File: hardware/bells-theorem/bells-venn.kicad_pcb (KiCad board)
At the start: 2 copper layers, 257.4 x 128.5 mm, 312 parts, among them J1 Conn_02x05_Odd_Even, J10 D, J11 C, J12 DA, J13 CD, J14 DAB, J15 CDA, J16 A, J17 B, J18 AB, J19 BC, J2 left, J20 ABC, J21 BCD, J22 left, J23 right, J3 right, J4 IN, J5 CVA, J6 CVB, J7 CVC, J8 CVD, J9 ABCD, Q1 Q_NPN_BCE, Q10 Q_NPN_BCE, Q12 Q_NPN_BCE, Q13 Q_NPN_BCE, Q3 Q_NPN_BCE, Q4 Q_NPN_BCE, Q6 Q_NPN_BCE, Q7 Q_NPN_BCE, Q9 Q_NPN_BCE, SW1 A, SW2 D, SW3 B, SW4 C, U1 Teensy4.1, U10 MCP47CVB12, U11 MCP47CVB12, U12 TL074, U13 TL074, U14 TL074, U15 TL072, U16 TL074, U17 TL074, U18 TL074, U19 TL074, U2 L7805, U20 TL074, U21 TL072, U3 L78L33_TO92, U4 PI4MSD5V9540B, U5 MCP47CVB11, U6 MCP47CVB12, U7 MCP47CVB12, U8 MCP47CVB12, U9 MCP47CVB12

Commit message: take gerbers out of the repo, push latest updates
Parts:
- removed the G*** at (60.7, 82.0)
- removed the G*** at (150.7, 81.9)
- removed the G*** at (60.7, 81.9)
- removed the REF** at (37.8, 36.1)
- removed the REF** at (83.3, 36.1)
- removed the REF** at (83.3, 80.7)
- removed the REF** at (258.1, 106.8)
- removed the REF** at (266.1, 102.0)
- removed the REF** at (216.3, 109.6)
- removed the REF** at (216.9, 101.7)
- removed the REF** at (37.8, 80.7)
- removed the REF** at (202.1, 109.0)
- removed the REF** at (203.8, 49.7)
- removed the REF** at (216.2, 43.4)
- removed the REF** at (204.5, 62.2)
- removed the REF** at (206.1, 75.8)
- removed the REF** at (217.4, 80.8)
- removed the REF** at (214.1, 84.6)
- removed the REF** at (214.2, 67.2)
- removed the REF** at (217.3, 56.4)
- removed the REF** at (214.1, 48.8)
- removed the REF** at (60.5, 80.8)
- removed the REF** at (219.5, 38.0)
- removed the REF** at (213.2, 31.1)
- removed the REF** at (218.4, 31.1)
- removed the REF** at (223.6, 31.1)
- removed the REF** at (265.7, 32.3)
- removed the REF** at (238.8, 38.2)
- removed the REF** at (244.9, 31.1)
- removed the REF** at (258.8, 31.2)
- removed the REF** at (254.3, 31.1)
- removed the REF** at (249.7, 31.2)
- removed the REF** at (250.7, 38.1)
- removed the REF** at (255.3, 38.2)
- removed the REF** at (274.4, 52.8)
- removed the REF** at (257.3, 42.0)
- removed the REF** at (257.4, 69.6)
- removed the REF** at (258.1, 85.2)
- removed the REF** at (257.3, 53.8)
- removed the REF** at (273.1, 60.1)
- removed the REF** at (273.1, 57.7)
- removed the REF** at (257.4, 58.8)
- removed the REF** at (262.1, 46.0)
- removed the REF** at (260.5, 49.7)
- removed the REF** at (262.4, 73.2)
- removed the REF** at (260.5, 77.0)
- removed the REF** at (262.9, 88.8)
- removed the REF** at (261.2, 92.7)
- removed SW1: A, Rotary_Encoder:RotaryEncoder_Alps_EC12E-Switch_Vertical_H20mm_CircularMountingHoles
- removed SW2: D, Rotary_Encoder:RotaryEncoder_Alps_EC12E-Switch_Vertical_H20mm_CircularMountingHoles
- removed SW3: B, Rotary_Encoder:RotaryEncoder_Alps_EC12E-Switch_Vertical_H20mm_CircularMountingHoles
- removed SW4: C, Rotary_Encoder:RotaryEncoder_Alps_EC12E-Switch_Vertical_H20mm_CircularMountingHoles
- removed U11: MCP47CVB12, Package_SO:MSOP-10_3x3mm_P0.5mm
- removed U12, U13, U14, U16, U17, U18: TL074, Package_SO:SOIC-14_3.9x8.7mm_P1.27mm
- removed U15: TL072, Package_SO:SOIC-8_3.9x4.9mm_P1.27mm
- added C10: 15nF, Capacitor_SMD:C_0805_2012Metric_Pad1.15x1.40mm_HandSolder, B.Cu at (253.5, 61.2)
- added C11: 15nF, Capacitor_SMD:C_0805_2012Metric_Pad1.15x1.40mm_HandSolder, B.Cu at (253.5, 79.0)
- added C12: 15nF, Capacitor_SMD:C_0805_2012Metric_Pad1.15x1.40mm_HandSolder, B.Cu at (253.5, 89.2)
- added C13: 15nF, Capacitor_SMD:C_0805_2012Metric_Pad1.15x1.40mm_HandSolder, B.Cu at (253.5, 66.0)
- added C14: 100nF, Capacitor_SMD:C_0805_2012Metric_Pad1.15x1.40mm_HandSolder, B.Cu at (261.9, 34.5)
- added C35: 100nF, Capacitor_SMD:C_0805_2012Metric_Pad1.15x1.40mm_HandSolder, B.Cu at (217.9, 47.2)
- added C36: 100nF, Capacitor_SMD:C_0805_2012Metric_Pad1.15x1.40mm_HandSolder, B.Cu at (217.9, 35.6)
- added C37: 100nF, Capacitor_SMD:C_0805_2012Metric_Pad1.15x1.40mm_HandSolder, B.Cu at (217.9, 65.3)
- added C38: 100nF, Capacitor_SMD:C_0805_2012Metric_Pad1.15x1.40mm_HandSolder, B.Cu at (217.9, 53.6)
- added C39: 100nF, Capacitor_SMD:C_0805_2012Metric_Pad1.15x1.40mm_HandSolder, B.Cu at (217.9, 81.5)
- added C7: 15nF, Capacitor_SMD:C_0805_2012Metric_Pad1.15x1.40mm_HandSolder, B.Cu at (253.3, 35.1)
- added C8: 15nF, Capacitor_SMD:C_0805_2012Metric_Pad1.15x1.40mm_HandSolder, B.Cu at (253.5, 51.1)
- added C9: 15nF, Capacitor_SMD:C_0805_2012Metric_Pad1.15x1.40mm_HandSolder, B.Cu at (253.4, 45.5)
- added G***: LOGO, My Library:bells-theorem-trefoil, F.Cu at (60.8, 58.3)
- added G***: LOGO, My Library:bells-theorem-just-inside-bmask, F.Cu at (60.8, 58.3)
- added G***: LOGO, My Library:bells-theorem-just-inside-fmask, F.Cu at (60.8, 58.3)
- added Q11: 2N3904, Package_TO_SOT_SMD:SOT-23_Handsoldering, F.Cu at (166.0, 91.2)
- added Q2: 2N3904, Package_TO_SOT_SMD:SOT-23_Handsoldering, F.Cu at (118.4, 48.7)
- added Q5: 2N3904, Package_TO_SOT_SMD:SOT-23_Handsoldering, F.Cu at (122.2, 91.2)
- added Q8: 2N3904, Package_TO_SOT_SMD:SOT-23_Handsoldering, F.Cu at (176.5, 47.4)
- added R11: 10K, Resistor_SMD:R_0805_2012Metric_Pad1.15x1.40mm_HandSolder, B.Cu at (253.4, 39.1)
- added R131: 390R, Resistor_SMD:R_0805_2012Metric_Pad1.15x1.40mm_HandSolder, F.Cu at (119.2, 43.8)
- added R14: 10K, Resistor_SMD:R_0805_2012Metric_Pad1.15x1.40mm_HandSolder, B.Cu at (253.4, 41.4)
- added R17: 10K, Resistor_SMD:R_0805_2012Metric_Pad1.15x1.40mm_HandSolder, B.Cu at (253.5, 55.1)
- added R20: 10K, Resistor_SMD:R_0805_2012Metric_Pad1.15x1.40mm_HandSolder, B.Cu at (253.5, 57.1)
- added R23: 10K, Resistor_SMD:R_0805_2012Metric_Pad1.15x1.40mm_HandSolder, B.Cu at (253.5, 83.1)
- added R26: 10K, Resistor_SMD:R_0805_2012Metric_Pad1.15x1.40mm_HandSolder, B.Cu at (253.5, 85.1)
- added R29: 10K, Resistor_SMD:R_0805_2012Metric_Pad1.15x1.40mm_HandSolder, B.Cu at (253.5, 70.6)
- added R32: 30K, Resistor_SMD:R_0805_2012Metric_Pad1.15x1.40mm_HandSolder, B.Cu at (253.4, 37.1)
- added REF**: stitch-via-0.6mm, My Library:stitch-via-0.6mm, F.Cu at (169.1, 90.2)
- added REF**: MountingHole_9mm_dia, My Library:MountingHole_9mm_dia, F.Cu at (38.3, 80.7)
- added REF**: MountingHole_9mm_dia, My Library:MountingHole_9mm_dia, F.Cu at (38.3, 35.8)
- added REF**: stitch-via-0.6mm, My Library:stitch-via-0.6mm, F.Cu at (260.9, 122.0)
- added REF**: stitch-via-0.6mm, My Library:stitch-via-0.6mm, F.Cu at (213.4, 113.4)
- added REF**: stitch-via-0.6mm, My Library:stitch-via-0.6mm, F.Cu at (246.9, 32.5)
- added REF**: stitch-via-0.6mm, My Library:stitch-via-0.6mm, F.Cu at (225.4, 87.8)
- added REF**: stitch-via-0.6mm, My Library:stitch-via-0.6mm, F.Cu at (263.9, 100.8)
- added REF**: stitch-via-0.6mm, My Library:stitch-via-0.6mm, F.Cu at (264.7, 95.8)
- added REF**: stitch-via-0.6mm, My Library:stitch-via-0.6mm, F.Cu at (205.5, 74.4)
- added REF**: stitch-via-0.6mm, My Library:stitch-via-0.6mm, F.Cu at (214.1, 66.5)
- added REF**: stitch-via-0.6mm, My Library:stitch-via-0.6mm, F.Cu at (206.2, 64.3)
- added REF**: stitch-via-0.6mm, My Library:stitch-via-0.6mm, F.Cu at (206.0, 55.1)
- added REF**: stitch-via-0.6mm, My Library:stitch-via-0.6mm, F.Cu at (212.1, 58.7)
- added REF**: stitch-via-0.6mm, My Library:stitch-via-0.6mm, F.Cu at (234.2, 89.7)
- added REF**: stitch-via-0.6mm, My Library:stitch-via-0.6mm, F.Cu at (218.7, 98.3)
- added REF**: stitch-via-0.6mm, My Library:stitch-via-0.6mm, F.Cu at (219.2, 52.3)
- added REF**: stitch-via-0.6mm, My Library:stitch-via-0.6mm, F.Cu at (213.1, 91.2)
- added REF**: stitch-via-0.6mm, My Library:stitch-via-0.6mm, F.Cu at (217.4, 85.1)
- added REF**: stitch-via-0.6mm, My Library:stitch-via-0.6mm, F.Cu at (214.6, 74.4)
- added REF**: MountingHole_9mm_dia, My Library:MountingHole_9mm_dia, F.Cu at (83.2, 80.7)
- added REF**: stitch-via-0.6mm, My Library:stitch-via-0.6mm, F.Cu at (220.2, 66.0)
- added REF**: stitch-via-0.6mm, My Library:stitch-via-0.6mm, F.Cu at (219.7, 60.5)
- added REF**: stitch-via-0.6mm, My Library:stitch-via-0.6mm, F.Cu at (218.9, 48.8)
- added REF**: stitch-via-0.6mm, My Library:stitch-via-0.6mm, F.Cu at (214.6, 40.1)
- added REF**: stitch-via-0.6mm, My Library:stitch-via-0.6mm, F.Cu at (258.8, 100.3)
- added REF**: stitch-via-0.6mm, My Library:stitch-via-0.6mm, F.Cu at (258.6, 82.8)
- added REF**: stitch-via-0.6mm, My Library:stitch-via-0.6mm, F.Cu at (258.6, 73.9)
- added REF**: stitch-via-0.6mm, My Library:stitch-via-0.6mm, F.Cu at (262.9, 32.8)
- added REF**: stitch-via-0.6mm, My Library:stitch-via-0.6mm, F.Cu at (262.9, 64.0)
- added REF**: stitch-via-0.6mm, My Library:stitch-via-0.6mm, F.Cu at (262.9, 48.3)
- added REF**: stitch-via-0.6mm, My Library:stitch-via-0.6mm, B.Cu at (258.6, 54.9)
- added REF**: stitch-via-0.6mm, My Library:stitch-via-0.6mm, F.Cu at (259.0, 39.1)
- added REF**: stitch-via-0.6mm, My Library:stitch-via-0.6mm, F.Cu at (161.6, 86.4)
- added REF**: stitch-via-0.6mm, My Library:stitch-via-0.6mm, F.Cu at (113.6, 37.7)
- added REF**: stitch-via-0.6mm, My Library:stitch-via-0.6mm, F.Cu at (144.4, 78.7)
- added REF**: stitch-via-0.6mm, My Library:stitch-via-0.6mm, F.Cu at (137.6, 67.7)
- added REF**: stitch-via-0.6mm, My Library:stitch-via-0.6mm, F.Cu at (178.6, 84.8)
- added REF**: stitch-via-0.6mm, My Library:stitch-via-0.6mm, F.Cu at (173.2, 90.8)
- added REF**: MountingHole_9mm_dia, My Library:MountingHole_9mm_dia, F.Cu at (83.2, 35.8)
- added REF**: stitch-via-0.6mm, My Library:stitch-via-0.6mm, F.Cu at (180.2, 48.6)
- added REF**: stitch-via-0.6mm, My Library:stitch-via-0.6mm, F.Cu at (131.6, 74.7)
- added S1: ENCODER-RGB-SWITCH, My Library:ENCODER_LED_3_KIT, F.Cu at (128.2, 35.7)
- added S2: ENCODER-RGB-SWITCH, My Library:ENCODER_LED_3_KIT, F.Cu at (128.2, 80.6)
- added S3: ENCODER-RGB-SWITCH, My Library:ENCODER_LED_3_KIT, F.Cu at (173.2, 35.7)
- added S4: ENCODER-RGB-SWITCH, My Library:ENCODER_LED_3_KIT, F.Cu at (173.2, 80.6)
- C22, C23, C24, C25, C26, C27: value 100nF -> 15nF
- Q1, Q10, Q12, Q13, Q3, Q4, Q6, Q7, Q9: value Q_NPN_BCE -> 2N3904
- R1, R12, R13, R18, R19, R2, R24, R25, R3, R30, R31, R4, R5, R6, R9: value R_US -> 4.7K
- R10, R15, R16, R21, R22, R27, R28, R33, R34: value R_US -> 470R
- R100, R101: value 4.7K -> 470R; moved to F.Cu
- R102, R103: moved to F.Cu
- R104: value 4.7K -> 15K
- R105: value 4.7K -> 390R; moved to F.Cu
- R106, R107, R35, R36, R37, R38, R39, R40, R70, R71, R72, R73: value 10K -> 30K
- R108, R109, R42, R43, R44, R45, R46, R47, R48, R76, R77, R78, R79, R80, R81: value 30K -> 10K
- R55, R56, R57, R58, R59, R60, R61, R86, R87, R88, R89, R90, R91: value 10K -> 220R
- R63, R64, R65, R66, R67: value 220R -> 10K
- R68, R69: value 220R -> 30K
- R7: value R_US -> 420R; moved to F.Cu
- R8: value R_US -> 470R; moved to F.Cu
- R92: value 10K -> 2.2K; moved to F.Cu
- R93: value 10K -> 4.7K; moved to F.Cu
- R94, R95, R96, R97, R98, R99: value 220R -> 4.7K
- U10, U6, U8, U9: value MCP47CVB12 -> TL074; footprint Package_SO:MSOP-10_3x3mm_P0.5mm -> Package_SO:SOIC-14_3.9x8.7mm_P1.27mm
- U2: value L7805 -> L78L05_TO92
- U4: value PI4MSD5V9540B -> TL074; footprint Package_SO:MSOP-8_3x3mm_P0.65mm -> Package_SO:SOIC-14_3.9x8.7mm_P1.27mm
- U5: value MCP47CVB11 -> TL074; footprint Package_SO:MSOP-10_3x3mm_P0.5mm -> Package_SO:SOIC-14_3.9x8.7mm_P1.27mm
- U7: value MCP47CVB12 -> TL072; footprint Package_SO:MSOP-10_3x3mm_P0.5mm -> Package_SO:SOIC-8_3.9x4.9mm_P1.27mm
- moved R105 122.9 mm to (117.2, 43.8), turned to 90 degrees
- moved R104 114.8 mm to (123.6, 35.8), turned to 270 degrees
- moved R103 108.9 mm to (169.1, 88.4)
- moved R92 88.4 mm to (121.4, 47.7), turned to 90 degrees
- moved R93 86.5 mm to (120.4, 88.3)
- moved R102 86.4 mm to (177.7, 44.6)
- moved R101 81.2 mm to (165.2, 88.3), turned to 0 degrees
- moved R68 72.2 mm to (222.2, 38.9), turned to 0 degrees
- moved R98 60.2 mm to (169.3, 35.8)
- moved R100 52.8 mm to (173.8, 44.6), turned to 180 degrees
- moved R62 49.6 mm to (222.3, 40.9), turned to 0 degrees
- moved R74 49.6 mm to (214.1, 35.6)
- moved U6 49.5 mm to (259.8, 84.0), turned to 180 degrees
- moved R7 48.9 mm to (121.3, 43.8), turned to 90 degrees
- moved C22 48.9 mm to (222.3, 36.8)
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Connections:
- C15 pad 1: +12V -> -12V
- C16 pad 1: -12V -> +12V
- C17 pad 1: +12V -> -12V
- C18 pad 1: -12V -> +12V
- C19 pad 1: +12V -> -12V
- C20 pad 1: -12V -> +12V
- C21 pad 1: +12V -> -12V
- C22 pad 1: -12V -> Net-(C22-Pad1)
- C22 pad 2: GND -> Net-(C22-Pad2)
- C23 pad 1: +12V -> Net-(C23-Pad1)
- C23 pad 2: GND -> Net-(C23-Pad2)
- C24 pad 1: -12V -> Net-(C24-Pad1)
- C24 pad 2: GND -> Net-(C24-Pad2)
- C25 pad 1: +12V -> Net-(C25-Pad1)
- C25 pad 2: GND -> Net-(C25-Pad2)
- C26 pad 1: -12V -> Net-(C26-Pad1)
- C26 pad 2: GND -> Net-(C26-Pad2)
- C27 pad 1: +12V -> Net-(C27-Pad1)
- C27 pad 2: GND -> Net-(C27-Pad2)
- C28 pad 1: -12V -> +12V
- J2 pad 10: /main/ENCD_B -> /main/CD
- J2 pad 11: /main/C -> /main/ENCD_B
- J2 pad 12: /main/B -> /main/ENCD_A
- J2 pad 13: /main/D -> /main/ENCD_SW
- J2 pad 14: /main/A -> /main/D
- J2 pad 3: /main/ENCA_A -> /main/ENCA_SW
- J2 pad 4: /main/ENCA_B -> /main/A
- J2 pad 5: /main/ENCA_SW -> /main/ENCA_B
- J2 pad 6: /main/DA -> /main/ENCA_A
- J2 pad 8: /main/ENCD_SW -> /main/DA
- J2 pad 9: /main/ENCD_A -> /main/CDA
- J22 pad 10: /main/ENCD_B -> /main/CD
- J22 pad 11: /main/C -> /main/ENCD_B
- J22 pad 12: /main/B -> /main/ENCD_A
- J22 pad 13: /main/D -> /main/ENCD_SW
- J22 pad 14: /main/A -> /main/D
- J22 pad 3: /main/ENCA_A -> /main/ENCA_SW
- J22 pad 4: /main/ENCA_B -> /main/A
- J22 pad 5: /main/ENCA_SW -> /main/ENCA_B
- J22 pad 6: /main/DA -> /main/ENCA_A
- J22 pad 8: /main/ENCD_SW -> /main/DA
- J22 pad 9: /main/ENCD_A -> /main/CDA
- J23 pad 10: /main/CDA -> /main/ABCD
- J23 pad 12: /main/CD -> /main/C
- J23 pad 13: /main/ENCC_A -> /main/ENCC_SW
- J23 pad 15: /main/ENCC_SW -> /main/ENCC_A
- J23 pad 3: /main/ENCB_SW -> /main/ENCB_B
- J23 pad 5: /main/ENCB_B -> /main/ENCB_SW
- J23 pad 6: /main/AB -> /main/B
- J23 pad 7: /main/ABC -> /main/AB
- J23 pad 8: /main/ABCD -> /main/ABC
- J3 pad 10: /main/CDA -> /main/ABCD
- J3 pad 12: /main/CD -> /main/C
- J3 pad 13: /main/ENCC_A -> /main/ENCC_SW
- J3 pad 15: /main/ENCC_SW -> /main/ENCC_A
- J3 pad 3: /main/ENCB_SW -> /main/ENCB_B
- J3 pad 5: /main/ENCB_B -> /main/ENCB_SW
- J3 pad 6: /main/AB -> /main/B
- J3 pad 7: /main/ABC -> /main/AB
- J3 pad 8: /main/ABCD -> /main/ABC
- Q1 pad 2: Net-(Q1-Pad2) -> Net-(D3-Pad2)
- Q1 pad 3: Net-(D3-Pad2) -> Net-(Q1-Pad3)
- Q10 pad 2: Net-(Q10-Pad2) -> Net-(D12-Pad2)
- Q10 pad 3: Net-(D12-Pad2) -> Net-(Q10-Pad3)
- Q12 pad 2: Net-(Q12-Pad2) -> Net-(D14-Pad2)
- Q12 pad 3: Net-(D14-Pad2) -> Net-(Q12-Pad3)
- Q13 pad 2: Net-(Q13-Pad2) -> Net-(D15-Pad2)
- Q13 pad 3: Net-(D15-Pad2) -> Net-(Q13-Pad3)
- Q3 pad 2: Net-(Q3-Pad2) -> Net-(D5-Pad2)
- Q3 pad 3: Net-(D5-Pad2) -> Net-(Q3-Pad3)
- Q4 pad 2: Net-(Q4-Pad2) -> Net-(D6-Pad2)
- Q4 pad 3: Net-(D6-Pad2) -> Net-(Q4-Pad3)
- Q6 pad 2: Net-(Q6-Pad2) -> Net-(D8-Pad2)
- Q6 pad 3: Net-(D8-Pad2) -> Net-(Q6-Pad3)
- Q7 pad 2: Net-(Q7-Pad2) -> Net-(D9-Pad2)
- Q7 pad 3: Net-(D9-Pad2) -> Net-(Q7-Pad3)
- Q9 pad 2: Net-(Q9-Pad2) -> Net-(D11-Pad2)
- Q9 pad 3: Net-(D11-Pad2) -> Net-(Q9-Pad3)
- R10 pad 2: Net-(Q1-Pad2) -> Net-(Q1-Pad3)
- R100 pad 1: +3V3 -> Net-(Q8-Pad3)
- R101 pad 1: +3V3 -> Net-(Q11-Pad3)
- R102 pad 1: +3V3 -> /main/B
- R102 pad 2: /main/rightI2C/right_SCL -> Net-(Q8-Pad1)
- R103 pad 1: +3V3 -> /main/C
- R103 pad 2: /main/rightI2C/right_SDA -> Net-(Q11-Pad1)
- R104 pad 1: +3V3 -> Net-(R104-Pad1)
- R104 pad 2: /main/LeftI2C/left_SCL -> /main/ENCA_SW
- R105 pad 1: +3V3 -> Net-(Q2-Pad3)
- R105 pad 2: /main/LeftI2C/left_SDA -> Net-(R105-Pad2)
- R15 pad 2: Net-(Q3-Pad2) -> Net-(Q3-Pad3)
- R16 pad 2: Net-(Q4-Pad2) -> Net-(Q4-Pad3)
- R21 pad 2: Net-(Q6-Pad2) -> Net-(Q6-Pad3)
- R22 pad 2: Net-(Q7-Pad2) -> Net-(Q7-Pad3)
- R27 pad 2: Net-(Q9-Pad2) -> Net-(Q9-Pad3)
- R28 pad 2: Net-(Q10-Pad2) -> Net-(Q10-Pad3)
- R33 pad 2: Net-(Q12-Pad2) -> Net-(Q12-Pad3)
- R34 pad 2: Net-(Q13-Pad2) -> Net-(Q13-Pad3)
- R35 pad 1: Net-(R35-Pad1) -> Net-(C8-Pad1)
- R35 pad 2: Net-(R35-Pad2) -> Net-(C8-Pad2)
- R36 pad 1: Net-(R36-Pad1) -> Net-(C11-Pad1)
- R36 pad 2: Net-(R36-Pad2) -> Net-(C11-Pad2)
- R37 pad 1: Net-(R37-Pad1) -> Net-(C9-Pad1)
- R37 pad 2: Net-(R37-Pad2) -> Net-(C9-Pad2)
- R38 pad 1: Net-(R38-Pad1) -> Net-(C10-Pad1)
- R38 pad 2: Net-(R38-Pad2) -> Net-(C10-Pad2)
- R39 pad 1: Net-(R39-Pad1) -> Net-(C12-Pad1)
- R39 pad 2: Net-(R39-Pad2) -> Net-(C12-Pad2)
- R40 pad 1: Net-(R40-Pad1) -> Net-(C13-Pad1)
- R40 pad 2: Net-(R40-Pad2) -> Net-(C13-Pad2)
- R41 pad 2: Net-(R41-Pad2) -> Net-(C7-Pad1)
- R42 pad 2: Net-(R35-Pad1) -> Net-(C9-Pad1)
- R43 pad 2: Net-(R37-Pad1) -> Net-(C8-Pad1)
- R44 pad 2: Net-(R39-Pad1) -> Net-(C10-Pad1)
- R45 pad 2: Net-(R36-Pad1) -> Net-(C11-Pad1)
- R46 pad 2: Net-(R38-Pad1) -> Net-(C12-Pad1)
- R47 pad 2: Net-(R40-Pad1) -> Net-(C13-Pad1)
- R48 pad 1: Net-(R48-Pad1) -> /main/B
- R49 pad 1: Net-(R49-Pad1) -> /main/ABC
- R49 pad 2: Net-(R42-Pad1) -> Net-(R43-Pad1)
- R5 pad 1: +3V3 -> /main/ENCA_SW
- R5 pad 2: /main/ENCB_B -> GND
- R50 pad 1: Net-(R50-Pad1) -> /main/BCD
- R51 pad 1: Net-(R51-Pad1) -> /main/AB
- R51 pad 2: Net-(R43-Pad1) -> Net-(R42-Pad1)
- R52 pad 1: Net-(R52-Pad1) -> /main/BC
- R52 pad 2: Net-(R46-Pad1) -> Net-(R44-Pad1)
- R53 pad 1: Net-(R53-Pad1) -> /main/C
- R53 pad 2: Net-(R44-Pad1) -> Net-(R46-Pad1)
- R54 pad 1: Net-(R54-Pad1) -> /main/ABCD
- R55 pad 1: Net-(R55-Pad1) -> /main/B
- R55 pad 2: Net-(R48-Pad1) -> Net-(R55-Pad2)
- R56 pad 2: Net-(R49-Pad1) -> Net-(R56-Pad2)
- R57 pad 1: /main/BC -> /main/ABC
- R57 pad 2: Net-(R51-Pad1) -> Net-(R57-Pad2)
- R58 pad 1: /main/BCD -> /main/BC
- R58 pad 2: Net-(R53-Pad1) -> Net-(R58-Pad2)
- R59 pad 1: /main/ABC -> /main/BCD
- R59 pad 2: Net-(R50-Pad1) -> Net-(R59-Pad2)
- R6 pad 1: +3V3 -> GND
- R6 pad 2: /main/ENCC_B -> /main/ENCD_SW
- R60 pad 1: /main/CDA -> /main/C
- R60 pad 2: Net-(R52-Pad1) -> Net-(R60-Pad2)
- R61 pad 1: /main/CD -> /main/ABCD
- R61 pad 2: Net-(R54-Pad1) -> Net-(R61-Pad2)
- R62 pad 1: /main/ABCD -> Net-(C22-Pad1)
- R62 pad 2: Net-(R55-Pad1) -> /main/left outs/A_in
- R63 pad 1: /main/AB -> Net-(C24-Pad1)
- R63 pad 2: Net-(R63-Pad2) -> /main/left outs/DA_in
- R64 pad 1: /main/ABC -> Net-(C23-Pad1)
- R64 pad 2: Net-(R64-Pad2) -> /main/left outs/DAB_in
- R65 pad 1: /main/BC -> Net-(C25-Pad1)
- R65 pad 2: Net-(R65-Pad2) -> /main/left outs/CDA_in
- R66 pad 1: /main/CDA -> Net-(C26-Pad1)
- R66 pad 2: Net-(R66-Pad2) -> /main/left outs/CD_in
- R67 pad 1: /main/BCD -> Net-(C27-Pad1)
- R67 pad 2: Net-(R67-Pad2) -> /main/left outs/D_in
- R68 pad 1: /main/CD -> Net-(C22-Pad2)
- R68 pad 2: Net-(R68-Pad2) -> Net-(C22-Pad1)
- R69 pad 1: /main/ABCD -> Net-(C24-Pad2)
- R69 pad 2: Net-(R69-Pad2) -> Net-(C24-Pad1)
- R7 pad 1: +3V3 -> Net-(Q2-Pad3)
- R7 pad 2: /main/ENCB_A -> Net-(R7-Pad2)
- R70 pad 1: Net-(R70-Pad1) -> Net-(C26-Pad2)
- R70 pad 2: Net-(R70-Pad2) -> Net-(C26-Pad1)
- R71 pad 1: Net-(R71-Pad1) -> Net-(C23-Pad2)
- R71 pad 2: Net-(R71-Pad2) -> Net-(C23-Pad1)
- R72 pad 1: Net-(R72-Pad1) -> Net-(C25-Pad2)
- R72 pad 2: Net-(R72-Pad2) -> Net-(C25-Pad1)
- R73 pad 1: Net-(R73-Pad1) -> Net-(C27-Pad2)
- R73 pad 2: Net-(R73-Pad2) -> Net-(C27-Pad1)
- R74 pad 2: Net-(R74-Pad2) -> Net-(C22-Pad2)
- R75 pad 2: Net-(R75-Pad2) -> Net-(C23-Pad2)
- R76 pad 2: Net-(R70-Pad1) -> Net-(C24-Pad2)
- R77 pad 2: Net-(R72-Pad1) -> Net-(C25-Pad2)
- R78 pad 2: Net-(R74-Pad1) -> Net-(C26-Pad2)
- R79 pad 2: Net-(R71-Pad1) -> Net-(C27-Pad2)
- R8 pad 1: +3V3 -> Net-(Q5-Pad3)
- R8 pad 2: /main/ENCC_A -> Net-(R8-Pad2)
- R80 pad 1: Net-(R80-Pad1) -> /main/A
- R80 pad 2: Net-(R73-Pad1) -> Net-(R74-Pad1)
- R81 pad 1: Net-(R81-Pad1) -> /main/DA
- R81 pad 2: Net-(R75-Pad1) -> Net-(R76-Pad1)
- R82 pad 1: Net-(R82-Pad1) -> /main/CD
- R82 pad 2: Net-(R76-Pad1) -> Net-(R78-Pad1)
- R83 pad 1: Net-(R83-Pad1) -> /main/DAB
- R83 pad 2: Net-(R79-Pad1) -> Net-(R75-Pad1)
- R84 pad 1: Net-(R84-Pad1) -> /main/CDA
- R85 pad 1: Net-(R85-Pad1) -> /main/D
- R85 pad 2: Net-(R80-Pad1) -> Net-(R79-Pad1)
- R86 pad 1: Net-(R86-Pad1) -> /main/A
- R86 pad 2: Net-(R78-Pad1) -> Net-(R86-Pad2)
- R87 pad 1: Net-(R87-Pad1) -> /main/DAB
- R87 pad 2: Net-(R81-Pad1) -> Net-(R87-Pad2)
- R88 pad 2: Net-(R82-Pad1) -> Net-(R88-Pad2)
- R89 pad 1: /main/C -> /main/CDA
- R89 pad 2: Net-(R84-Pad1) -> Net-(R89-Pad2)
- R90 pad 1: /main/D -> /main/CD
- R90 pad 2: Net-(R86-Pad1) -> Net-(R90-Pad2)
- R91 pad 1: /main/DAB -> /main/D
- R91 pad 2: Net-(R83-Pad1) -> Net-(R91-Pad2)
- R92 pad 1: /main/B -> /main/A
- R92 pad 2: Net-(R85-Pad1) -> Net-(Q2-Pad1)
- R93 pad 1: /main/A -> /main/D
- R93 pad 2: Net-(R87-Pad1) -> Net-(Q5-Pad1)
- R94 pad 1: /main/DA -> +3V3
- R94 pad 2: Net-(R94-Pad2) -> /main/ENCB_B
- R95 pad 1: /main/DAB -> +3V3
- R95 pad 2: Net-(R95-Pad2) -> /main/ENCC_B
- R96 pad 1: /main/C -> +3V3
- R96 pad 2: Net-(R96-Pad2) -> /main/ENCB_A
- R97 pad 1: /main/B -> +3V3
- R97 pad 2: Net-(R97-Pad2) -> /main/ENCC_A
- R98 pad 1: /main/D -> /main/ENCB_SW
- R98 pad 2: Net-(R98-Pad2) -> GND
- R99 pad 1: /main/A -> GND
- R99 pad 2: Net-(R99-Pad2) -> /main/ENCC_SW
- U1 pad 10: Net-(U1-Pad10) -> /main/right outs/ABC_in
- U1 pad 11: Net-(U1-Pad11) -> /main/right outs/BC_in
- U1 pad 16: /main/scaleright/CVC_out -> /main/right outs/ABCD_in
- U1 pad 17: /main/scaleright/CVD_out -> /main/right outs/BCD_in
- U1 pad 18: Net-(U1-Pad18) -> /main/scaleright/CVC_out
- U1 pad 19: Net-(U1-Pad19) -> /main/scaleright/CVD_out
- U1 pad 2: /main/LeftI2C/~LAT -> /main/ENCB_B
- U1 pad 20: Net-(U1-Pad20) -> /main/right outs/C_in
- U1 pad 21: Net-(U1-Pad21) -> /main/left outs/D_in
- U1 pad 25: Net-(U1-Pad25) -> /main/left outs/CD_in
- U1 pad 28: Net-(U1-Pad28) -> /main/left outs/CDA_in
- U1 pad 29: Net-(U1-Pad29) -> /main/left outs/DA_in
- U1 pad 3: /main/ENCB_SW -> /main/ENCB_A
- U1 pad 36: /main/ENCD_B -> /main/ENCD_SW
- U1 pad 38: /main/ENCD_SW -> /main/ENCD_B
- U1 pad 39: Net-(U1-Pad39) -> /main/ENCA_A
- U1 pad 4: /main/ENCB_A -> /main/ENCB_SW
- U1 pad 40: Net-(R100-Pad2) -> /main/ENCA_B
- U1 pad 41: Net-(R101-Pad2) -> /main/ENCA_SW
- U1 pad 43: /main/ENCA_SW -> Net-(U1-Pad43)
- U1 pad 44: /main/ENCA_B -> /main/left outs/DAB_in
- U1 pad 45: /main/ENCA_A -> /main/left outs/A_in
- U1 pad 5: /main/ENCB_B -> /main/ENCC_SW
- U1 pad 6: /main/ENCC_A -> /main/ENCC_B
- U1 pad 7: /main/ENCC_B -> /main/ENCC_A
- U1 pad 8: /main/ENCC_SW -> /main/right outs/B_in
- U1 pad 9: Net-(U1-Pad9) -> /main/right outs/AB_in
- U10 pad 1: +3V3 -> Net-(C26-Pad2)
- U10 pad 10: /main/LeftI2C/left_SDA -> GND
- U10 pad 2: GND -> Net-(C26-Pad1)
- U10 pad 3: Net-(U10-Pad3) -> GND
- U10 pad 4: Net-(R73-Pad2) -> +12V
- U10 pad 5: Net-(R72-Pad2) -> GND
- U10 pad 6: /main/LeftI2C/~LAT -> Net-(C27-Pad1)
- U10 pad 7: GND -> Net-(C27-Pad2)
- U10 pad 8: +3V3 -> Net-(R91-Pad2)
- U10 pad 9: /main/LeftI2C/left_SCL -> Net-(R79-Pad1)
- U2 pad 1: +12V -> +5V
- U2 pad 3: +5V -> +12V
- U4 pad 1: Net-(R101-Pad2) -> Net-(R55-Pad2)
- U4 pad 2: Net-(R100-Pad2) -> Net-(R41-Pad1)
- U4 pad 3: +3V3 -> GND
- U4 pad 4: /main/LeftI2C/left_SDA -> +12V
- U4 pad 5: /main/LeftI2C/left_SCL -> GND
- U4 pad 6: GND -> Net-(R42-Pad1)
- U4 pad 7: /main/rightI2C/right_SDA -> Net-(R56-Pad2)
- U4 pad 8: /main/rightI2C/right_SCL -> Net-(C9-Pad1)
- U5 pad 1: +3V3 -> Net-(R57-Pad2)
- U5 pad 10: /main/rightI2C/right_SDA -> GND
- U5 pad 2: GND -> Net-(R43-Pad1)
- U5 pad 3: Net-(U5-Pad3) -> GND
- U5 pad 4: Net-(R41-Pad2) -> +12V
- U5 pad 5: Net-(U5-Pad5) -> GND
- U5 pad 6: /main/LeftI2C/~LAT -> Net-(R44-Pad1)
- U5 pad 7: GND -> Net-(R58-Pad2)
- U5 pad 8: GND -> Net-(C10-Pad1)
- U5 pad 9: /main/rightI2C/right_SCL -> Net-(C10-Pad2)
- U6 pad 1: +3V3 -> Net-(R59-Pad2)
- U6 pad 10: /main/rightI2C/right_SDA -> GND
- U6 pad 2: +3V3 -> Net-(R45-Pad1)
- U6 pad 3: Net-(U6-Pad3) -> GND
- U6 pad 4: Net-(R35-Pad2) -> +12V
- U6 pad 5: Net-(R36-Pad2) -> GND
- U6 pad 6: /main/LeftI2C/~LAT -> Net-(R46-Pad1)
- U6 pad 7: GND -> Net-(R60-Pad2)
- U6 pad 8: +3V3 -> Net-(C12-Pad1)
- U6 pad 9: /main/rightI2C/right_SCL -> Net-(C12-Pad2)
- U7 pad 1: +3V3 -> Net-(R61-Pad2)
- U7 pad 2: GND -> Net-(R47-Pad1)
- U7 pad 3: Net-(U7-Pad3) -> GND
- U7 pad 4: Net-(R37-Pad2) -> -12V
- U7 pad 5: Net-(R38-Pad2) -> GND
- U7 pad 6: /main/LeftI2C/~LAT -> Net-(C13-Pad2)
- U7 pad 7: GND -> Net-(C13-Pad1)
- U7 pad 8: +3V3 -> +12V
- U8 pad 1: +3V3 -> Net-(C22-Pad2)
- U8 pad 10: /main/rightI2C/right_SDA -> GND
- U8 pad 2: +3V3 -> Net-(C22-Pad1)
- U8 pad 3: Net-(U8-Pad3) -> GND
- U8 pad 4: Net-(R39-Pad2) -> +12V
- U8 pad 5: Net-(R40-Pad2) -> GND
- U8 pad 6: /main/LeftI2C/~LAT -> Net-(C23-Pad1)
- U8 pad 7: GND -> Net-(C23-Pad2)
- U8 pad 8: GND -> Net-(R87-Pad2)
- U8 pad 9: /main/rightI2C/right_SCL -> Net-(R75-Pad1)
- U9 pad 1: +3V3 -> Net-(C24-Pad2)
- U9 pad 10: /main/LeftI2C/left_SDA -> GND
- U9 pad 2: +3V3 -> Net-(C24-Pad1)
- U9 pad 3: Net-(U9-Pad3) -> GND
- U9 pad 4: Net-(R71-Pad2) -> +12V
- U9 pad 5: Net-(R70-Pad2) -> GND
- U9 pad 6: /main/LeftI2C/~LAT -> Net-(C25-Pad1)
- U9 pad 7: GND -> Net-(C25-Pad2)
- U9 pad 8: +3V3 -> Net-(R89-Pad2)
- U9 pad 9: /main/LeftI2C/left_SCL -> Net-(R77-Pad1)
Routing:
- net /main/B: track 49.1 -> 122.6 mm
- net /main/LeftI2C/~LAT: track 69.3 -> 0.00 mm, vias 12 -> 0
- net Net-(R40-Pad2): track 60.5 -> 0.00 mm
- net Net-(R39-Pad2): track 56.6 -> 0.00 mm
- net Net-(R75-Pad2): track 52.4 -> 0.00 mm
- net Net-(R74-Pad2): track 49.3 -> 0.00 mm
- net /main/C: track 66.8 -> 113.8 mm, vias 1 -> 0
- net Net-(R38-Pad2): track 42.4 -> 0.00 mm
- net /main/ENCC_SW: track 49.6 -> 91.2 mm
- net Net-(R37-Pad2): track 39.1 -> 0.00 mm
- net /main/left outs/D_in: track 0.00 -> 38.1 mm
- net /main/LeftI2C/left_SCL: track 37.6 -> 0.00 mm, vias 2 -> 0
- net Net-(R73-Pad2): track 36.8 -> 0.00 mm
- net /main/LeftI2C/left_SDA: track 35.3 -> 0.00 mm
- net /main/rightI2C/right_SCL: track 35.2 -> 0.00 mm
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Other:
- board text added: ">"
- board text added: "All transistors 2N3904 or equivalent"
- board text added: "Bell’s Theorem prototype 0.2"
- board text added: "Bell’s Theorem prototype 0.3"
- board text added: "Copyright (c) 2020 Frogleg Synthesis"
- board text added: "Thanks to Nyles Miszczyk for the inspiration to make this"
- board text added: "enca_a"
- board text added: "enca_b"
- board text added: "enca_sw"
- board text added: "encb_a"
- board text added: "encb_b"
- board text added: "encb_sw"
- board text added: "encc_a"
- board text added: "encc_b"
- board text added: "encc_sw"
- board text added: "encd_a"
- board text added: "encd_b"
- board text added: "encd_sw"
- board text removed: "0x60"
- board text removed: "0x61"
- board text removed: "0x62"
- board text removed: "0x63"
- board text removed: "0x70"
- board text removed: "Bell’s Theorem prototype 0.1"
- board text removed: "X"
- board text removed: "if I switch to sparkfun LED encoders, need 8.6mm holes"

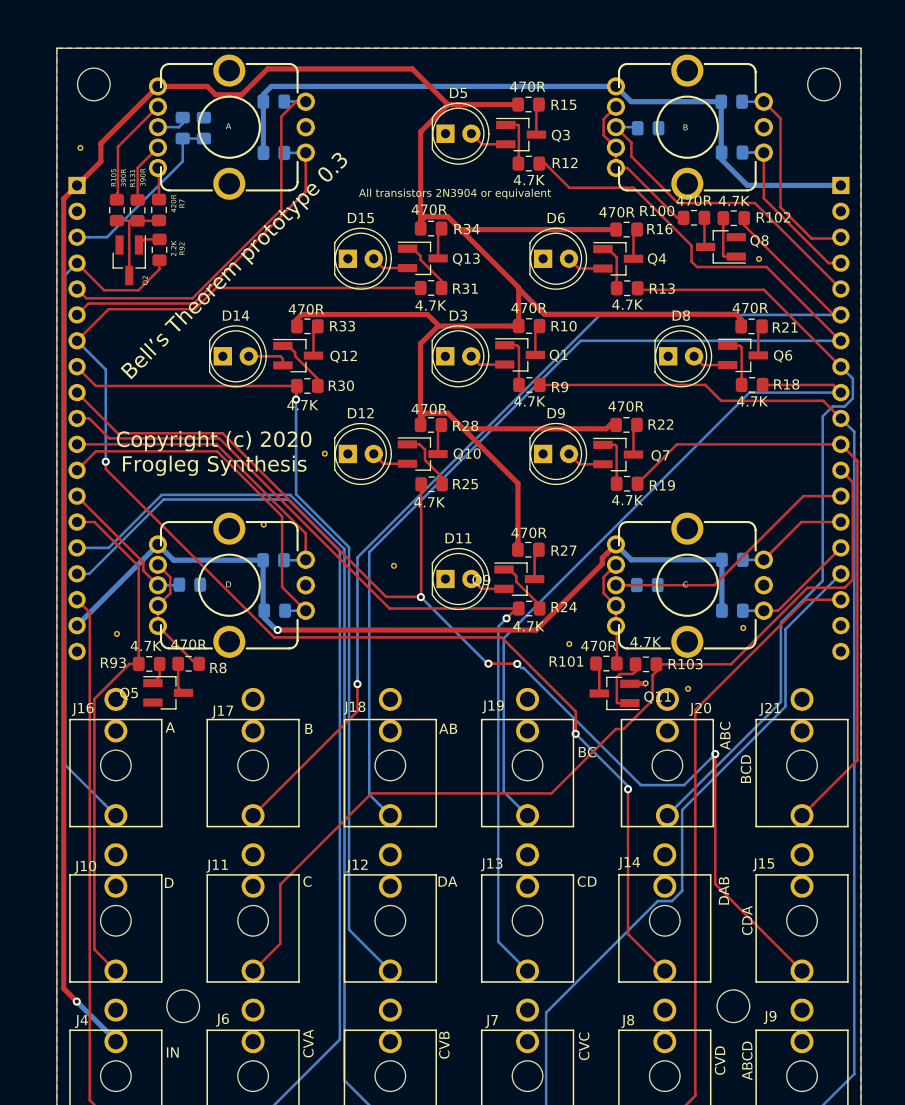
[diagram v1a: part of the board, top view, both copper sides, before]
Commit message: revised LED drivers for encoders, fixed code in various places
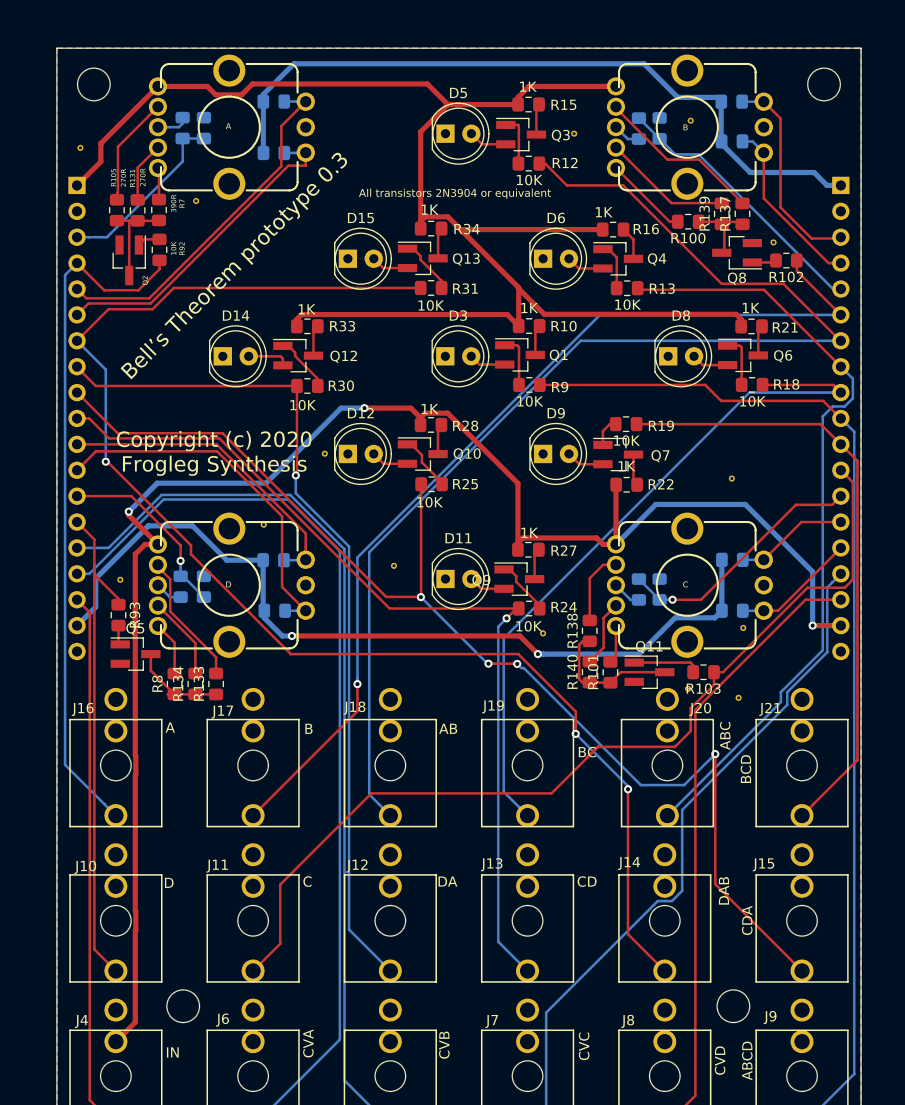
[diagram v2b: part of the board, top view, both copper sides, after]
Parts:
- added R132: 15K, Resistor_SMD:R_0805_2012Metric_Pad1.15x1.40mm_HandSolder, B.Cu at (123.4, 80.8)
- added R133: 270R, Resistor_SMD:R_0805_2012Metric_Pad1.15x1.40mm_HandSolder, F.Cu at (126.9, 90.3)
- added R134: 270R, Resistor_SMD:R_0805_2012Metric_Pad1.15x1.40mm_HandSolder, F.Cu at (124.9, 90.3)
- added R135: 15K, Resistor_SMD:R_0805_2012Metric_Pad1.15x1.40mm_HandSolder, B.Cu at (168.4, 81.0)
- added R136: 15K, Resistor_SMD:R_0805_2012Metric_Pad1.15x1.40mm_HandSolder, B.Cu at (168.4, 35.8)
- added R137: 270R, Resistor_SMD:R_0805_2012Metric_Pad1.15x1.40mm_HandSolder, F.Cu at (178.6, 44.2)
- added R138: 270R, Resistor_SMD:R_0805_2012Metric_Pad1.15x1.40mm_HandSolder, F.Cu at (163.6, 85.1)
- added R139: 270R, Resistor_SMD:R_0805_2012Metric_Pad1.15x1.40mm_HandSolder, F.Cu at (176.5, 44.2)
- added R140: 270R, Resistor_SMD:R_0805_2012Metric_Pad1.15x1.40mm_HandSolder, F.Cu at (163.6, 89.1)
- added REF**: stitch-via-0.6mm, My Library:stitch-via-0.6mm, F.Cu at (177.5, 70.2)
- added REF**: stitch-via-0.6mm, My Library:stitch-via-0.6mm, F.Cu at (173.5, 35.1)
- added REF**: stitch-via-0.6mm, My Library:stitch-via-0.6mm, F.Cu at (162.1, 36.3)
- added REF**: stitch-via-0.6mm, My Library:stitch-via-0.6mm, F.Cu at (125.0, 42.9)
- R10, R15, R16, R21, R22, R27, R28, R33, R34: value 470R -> 1K
- R100, R101, R8: value 470R -> 390R
- R102, R103, R12, R13, R18, R19, R24, R25, R30, R31, R9, R93: value 4.7K -> 10K
- R105, R131: value 390R -> 270R
- R7: value 420R -> 390R
- R92: value 2.2K -> 10K
- moved REF** 9.23 mm to (178.2, 91.7)
- moved R102 6.63 mm to (182.9, 48.8)
- moved R22 5.87 mm to (167.2, 70.8)
- moved R19 5.84 mm to (167.1, 64.8)
- moved R103 5.70 mm to (174.7, 89.2)
- moved R93 5.65 mm to (117.3, 83.6), turned to 270 degrees
- moved REF** 5.32 mm to (117.5, 80.1)
- moved Q5 4.97 mm to (119.0, 87.4)
- moved Q11 4.01 mm to (169.4, 89.2), turned to 0 degrees
- moved REF** 2.77 mm to (159.0, 85.3)
- moved R8 2.41 mm to (122.9, 90.3), turned to 90 degrees
- moved REF** 2.16 mm to (181.6, 47.0)
- moved Q8 1.68 mm to (178.0, 48.0)
- moved R6 1.40 mm to (125.7, 80.8), turned to 270 degrees
- moved R16 1.33 mm to (165.9, 45.7)
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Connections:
- S2 pad 2: Net-(R8-Pad2) -> Net-(R134-Pad2)
- S2 pad 3: /main/ENCD_SW -> Net-(R132-Pad1)
- S2 pad 4: Net-(R8-Pad2) -> Net-(R133-Pad2)
- S2 pad 5: +3V3 -> +12V
- S3 pad 2: Net-(R100-Pad2) -> Net-(R139-Pad2)
- S3 pad 3: /main/ENCB_SW -> Net-(R136-Pad1)
- S3 pad 4: Net-(R100-Pad2) -> Net-(R137-Pad2)
- S3 pad 5: +3V3 -> +12V
- S4 pad 2: Net-(R101-Pad2) -> Net-(R140-Pad2)
- S4 pad 3: /main/ENCC_SW -> Net-(R135-Pad1)
- S4 pad 4: Net-(R101-Pad2) -> Net-(R138-Pad2)
- S4 pad 5: +3V3 -> +12V
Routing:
- net +12V: track 654.4 -> 687.0 mm, vias 19 -> 21
- net Net-(R137-Pad2): track 0.00 -> 16.6 mm
- net Net-(R133-Pad2): track 0.00 -> 13.6 mm
- net Net-(R139-Pad2): track 0.00 -> 13.0 mm
- net Net-(Q11-Pad3): track 3.07 -> 13.5 mm
- net Net-(R134-Pad2): track 0.00 -> 8.36 mm
- net Net-(R100-Pad2): track 15.7 -> 8.24 mm
- net Net-(R138-Pad2): track 0.00 -> 7.26 mm
- net Net-(R8-Pad2): track 12.6 -> 5.52 mm
- net Net-(R101-Pad2): track 10.7 -> 3.74 mm
- net /main/B: track 122.6 -> 115.9 mm
- net Net-(Q5-Pad3): track 3.06 -> 9.69 mm
- net Net-(R140-Pad2): track 0.00 -> 6.57 mm
- net /main/ENCB_SW: track 82.0 -> 77.1 mm
- net Net-(Q8-Pad3): track 2.90 -> 7.70 mm
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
